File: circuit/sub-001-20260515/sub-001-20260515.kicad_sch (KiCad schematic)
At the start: 5 parts

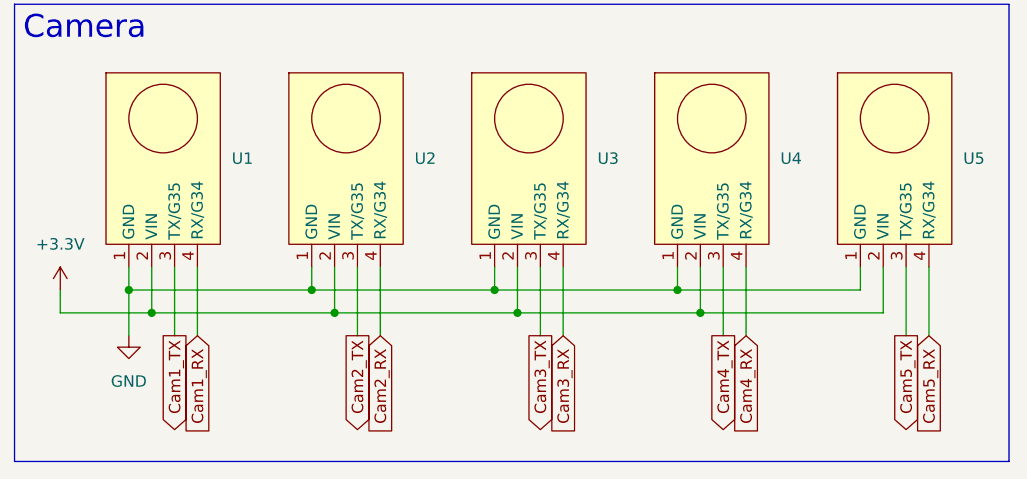
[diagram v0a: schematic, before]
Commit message: Update カメラのRX/TXを修正
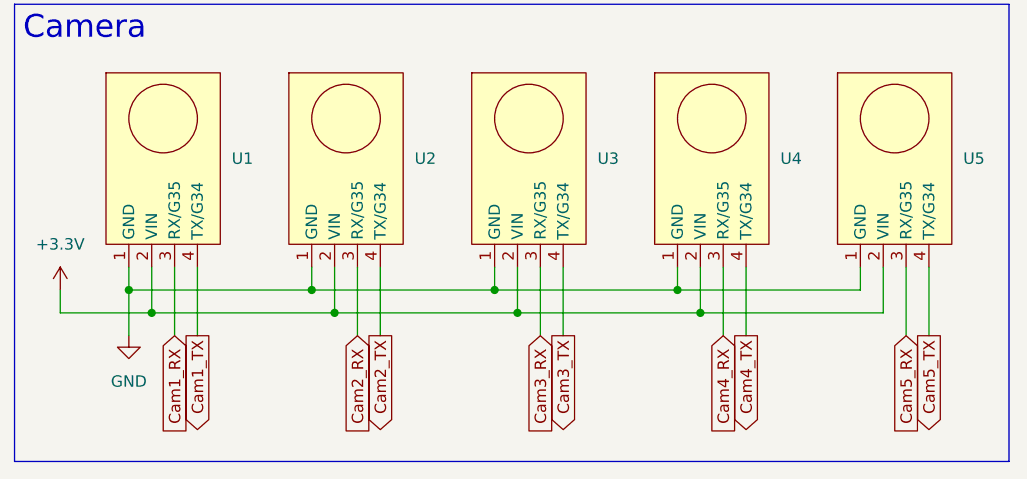
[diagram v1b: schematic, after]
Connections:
- net Cam1_RX: now also U1.3 (RX/G35); no longer U1.4 (RX/G34)
- net Cam1_TX: now also U1.4 (TX/G34); no longer U1.3 (TX/G35)
- net Cam2_RX: now also U2.3 (RX/G35); no longer U2.4 (RX/G34)
- net Cam2_TX: now also U2.4 (TX/G34); no longer U2.3 (TX/G35)
- net Cam3_RX: now also U3.3 (RX/G35); no longer U3.4 (RX/G34)
- net Cam3_TX: now also U3.4 (TX/G34); no longer U3.3 (TX/G35)
- net Cam4_RX: now also U4.3 (RX/G35); no longer U4.4 (RX/G34)
- net Cam4_TX: now also U4.4 (TX/G34); no longer U4.3 (TX/G35)
- net Cam5_RX: now also U5.3 (RX/G35); no longer U5.4 (RX/G34)
- net Cam5_TX: now also U5.4 (TX/G34); no longer U5.3 (TX/G35)
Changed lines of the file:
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@@
 	(global_label "Cam5_TX"
 		(shape output)
+		(at 114.3 49.53 270)
+		(fields_autoplaced yes)
+		(effects
+			(font
+				(size 1.27 1.27)
+			)
+			(justify right)
+		)
+		(property "Intersheetrefs" "${INTERSHEET_REFS}"
+			(at 114.3 61.3763 90)
+			(hide yes)
+			(show_name no)
+			(do_not_autoplace no)
+			(effects
+				(font
+					(size 1.27 1.27)
+				)
+				(justify right)
+			)
+		)
+	)
+	(global_label "Cam1_RX"
+		(shape input)
+		(at 30.48 49.53 270)
+		(fields_autoplaced yes)
+		(effects
+			(font
+				(size 1.27 1.27)
+			)
+			(justify right)
+		)
+		(property "Intersheetrefs" "${INTERSHEET_REFS}"
+			(at 30.48 61.4756 90)
+			(hide yes)
+			(show_name no)
+			(do_not_autoplace no)
+			(effects
+				(font
+					(size 1.27 1.27)
+				)
+				(justify right)
+			)
+		)
+	)
+	(global_label "Cam3_TX"
+		(shape output)
+		(at 73.66 49.53 270)
+		(fields_autoplaced yes)
+		(effects
+			(font
+				(size 1.27 1.27)
+			)
+			(justify right)
+		)
+		(property "Intersheetrefs" "${INTERSHEET_REFS}"
+			(at 73.66 61.3763 90)
+			(hide yes)
+			(show_name no)
+			(do_not_autoplace no)
+			(effects
+				(font
+					(size 1.27 1.27)
+				)
+				(justify right)
+			)
+		)
+	)
+	(global_label "Cam2_TX"
+		(shape output)
+		(at 53.34 49.53 270)
+		(fields_autoplaced yes)
+		(effects
+			(font
+				(size 1.27 1.27)
+			)
+			(justify right)
+		)
+		(property "Intersheetrefs" "${INTERSHEET_REFS}"
+			(at 53.34 61.3763 90)
+			(hide yes)
+			(show_name no)
+			(do_not_autoplace no)
+			(effects
+				(font
+					(size 1.27 1.27)
+				)
+				(justify right)
+			)
+		)
+	)
+	(global_label "Cam2_RX"
+		(shape input)
+		(at 50.8 49.53 270)
+		(fields_autoplaced yes)
+		(effects
+			(font
+				(size 1.27 1.27)
+			)
+			(justify right)
+		)
+		(property "Intersheetrefs" "${INTERSHEET_REFS}"
+			(at 50.8 61.4756 90)
+			(hide yes)
+			(show_name no)
+			(do_not_autoplace no)
+			(effects
+				(font
+					(size 1.27 1.27)
+				)
+				(justify right)
+			)
+		)
+	)
+	(global_label "Cam5_RX"
+		(shape input)
 		(at 111.76 49.53 270)
 		(fields_autoplaced yes)
@@
 		)
 		(property "Intersheetrefs" "${INTERSHEET_REFS}"
-			(at 111.76 61.3763 90)
-			(hide yes)
-			(show_name no)
-			(do_not_autoplace no)
-			(effects
-				(font
-					(size 1.27 1.27)
-				)
-				(justify right)
-			)
-		)
-	)
-	(global_label "Cam1_RX"
-		(shape input)
+			(at 111.76 61.4756 90)
+			(hide yes)
+			(show_name no)
+			(do_not_autoplace no)
+			(effects
+				(font
+					(size 1.27 1.27)
+				)
+				(justify right)
+			)
+		)
+	)
+	(global_label "Cam3_RX"
+		(shape input)
+		(at 71.12 49.53 270)
+		(fields_autoplaced yes)
+		(effects
+			(font
+				(size 1.27 1.27)
+			)
+			(justify right)
+		)
+		(property "Intersheetrefs" "${INTERSHEET_REFS}"
+			(at 71.12 61.4756 90)
+			(hide yes)
+			(show_name no)
+			(do_not_autoplace no)
+			(effects
+				(font
+					(size 1.27 1.27)
+				)
+				(justify right)
+			)
+		)
+	)
+	(global_label "Cam4_TX"
+		(shape output)
+		(at 93.98 49.53 270)
+		(fields_autoplaced yes)
+		(effects
+			(font
+				(size 1.27 1.27)
+			)
+			(justify right)
+		)
+		(property "Intersheetrefs" "${INTERSHEET_REFS}"
+			(at 93.98 61.3763 90)
+			(hide yes)
+			(show_name no)
+			(do_not_autoplace no)
+			(effects
+				(font
+					(size 1.27 1.27)
+				)
+				(justify right)
+			)
+		)
+	)
+	(global_label "Cam4_RX"
+		(shape input)
+		(at 91.44 49.53 270)
+		(fields_autoplaced yes)
+		(effects
+			(font
+				(size 1.27 1.27)
+			)
+			(justify right)
+		)
+		(property "Intersheetrefs" "${INTERSHEET_REFS}"
+			(at 91.44 61.4756 90)
+			(hide yes)
+			(show_name no)
+			(do_not_autoplace no)
+			(effects
+				(font
+					(size 1.27 1.27)
+				)
+				(justify right)
+			)
+		)
+	)
+	(global_label "Cam1_TX"
+		(shape output)
 		(at 33.02 49.53 270)
 		(fields_autoplaced yes)
@@
 		)
 		(property "Intersheetrefs" "${INTERSHEET_REFS}"
-			(at 33.02 61.4756 90)
-			(hide yes)
-			(show_name no)
-			(do_not_autoplace no)
-			(effects
-				(font
-					(size 1.27 1.27)
-				)
-				(justify right)
-			)
-		)
-	)
-	(global_label "Cam3_TX"
-		(shape output)
-		(at 71.12 49.53 270)
-		(fields_autoplaced yes)
-		(effects
-			(font
-				(size 1.27 1.27)
-			)
-			(justify right)
-		)
-		(property "Intersheetrefs" "${INTERSHEET_REFS}"
-			(at 71.12 61.3763 90)
-			(hide yes)
-			(show_name no)
-			(do_not_autoplace no)
-			(effects
-				(font
-					(size 1.27 1.27)
-				)
-				(justify right)
-			)
-		)
-	)
-	(global_label "Cam2_TX"
-		(shape output)
-		(at 50.8 49.53 270)
-		(fields_autoplaced yes)
-		(effects
-			(font
-				(size 1.27 1.27)
-			)
-			(justify right)
-		)
-		(property "Intersheetrefs" "${INTERSHEET_REFS}"
-			(at 50.8 61.3763 90)
-			(hide yes)
-			(show_name no)
-			(do_not_autoplace no)
-			(effects
-				(font
-					(size 1.27 1.27)
-				)
-				(justify right)
-			)
-		)
-	)
-	(global_label "Cam2_RX"
-		(shape input)
-		(at 53.34 49.53 270)
-		(fields_autoplaced yes)
-		(effects
-			(font
-				(size 1.27 1.27)
-			)
-			(justify right)
-		)
-		(property "Intersheetrefs" "${INTERSHEET_REFS}"
-			(at 53.34 61.4756 90)
-			(hide yes)
-			(show_name no)
-			(do_not_autoplace no)
-			(effects
-				(font
-					(size 1.27 1.27)
-				)
-				(justify right)
-			)
-		)
-	)
-	(global_label "Cam5_RX"
-		(shape input)
-		(at 114.3 49.53 270)
-		(fields_autoplaced yes)
-		(effects
-			(font
-				(size 1.27 1.27)
-			)
-			(justify right)
-		)
-		(property "Intersheetrefs" "${INTERSHEET_REFS}"
-			(at 114.3 61.4756 90)
-			(hide yes)
-			(show_name no)
-			(do_not_autoplace no)
-			(effects
-				(font
-					(size 1.27 1.27)
-				)
-				(justify right)
-			)
-		)
-	)
-	(global_label "Cam3_RX"
-		(shape input)
-		(at 73.66 49.53 270)
-		(fields_autoplaced yes)
-		(effects
-			(font
-				(size 1.27 1.27)
-			)
-			(justify right)
-		)
-		(property "Intersheetrefs" "${INTERSHEET_REFS}"
-			(at 73.66 61.4756 90)
-			(hide yes)
-			(show_name no)
-			(do_not_autoplace no)
-			(effects
-				(font
-					(size 1.27 1.27)
-				)
-				(justify right)
-			)
-		)
-	)
-	(global_label "Cam4_TX"
-		(shape output)
-		(at 91.44 49.53 270)
-		(fields_autoplaced yes)
-		(effects
-			(font
-				(size 1.27 1.27)
-			)
-			(justify right)
-		)
-		(property "Intersheetrefs" "${INTERSHEET_REFS}"
-			(at 91.44 61.3763 90)
-			(hide yes)
-			(show_name no)
-			(do_not_autoplace no)
-			(effects
-				(font
-					(size 1.27 1.27)
-				)
-				(justify right)
-			)
-		)
-	)
-	(global_label "Cam4_RX"
-		(shape input)
-		(at 93.98 49.53 270)
-		(fields_autoplaced yes)
-		(effects
-			(font
-				(size 1.27 1.27)
-			)
-			(justify right)
-		)
-		(property "Intersheetrefs" "${INTERSHEET_REFS}"
-			(at 93.98 61.4756 90)
-			(hide yes)
-			(show_name no)
-			(do_not_autoplace no)
-			(effects
-				(font
-					(size 1.27 1.27)
-				)
-				(justify right)
-			)
-		)
-	)
-	(global_label "Cam1_TX"
-		(shape output)
-		(at 30.48 49.53 270)
-		(fields_autoplaced yes)
-		(effects
-			(font
-				(size 1.27 1.27)
-			)
-			(justify right)
-		)
-		(property "Intersheetrefs" "${INTERSHEET_REFS}"
-			(at 30.48 61.3763 90)
-			(hide yes)
-			(show_name no)
+			(at 33.02 61.3763 90)
+			(hide yes)
+			(show_name no)

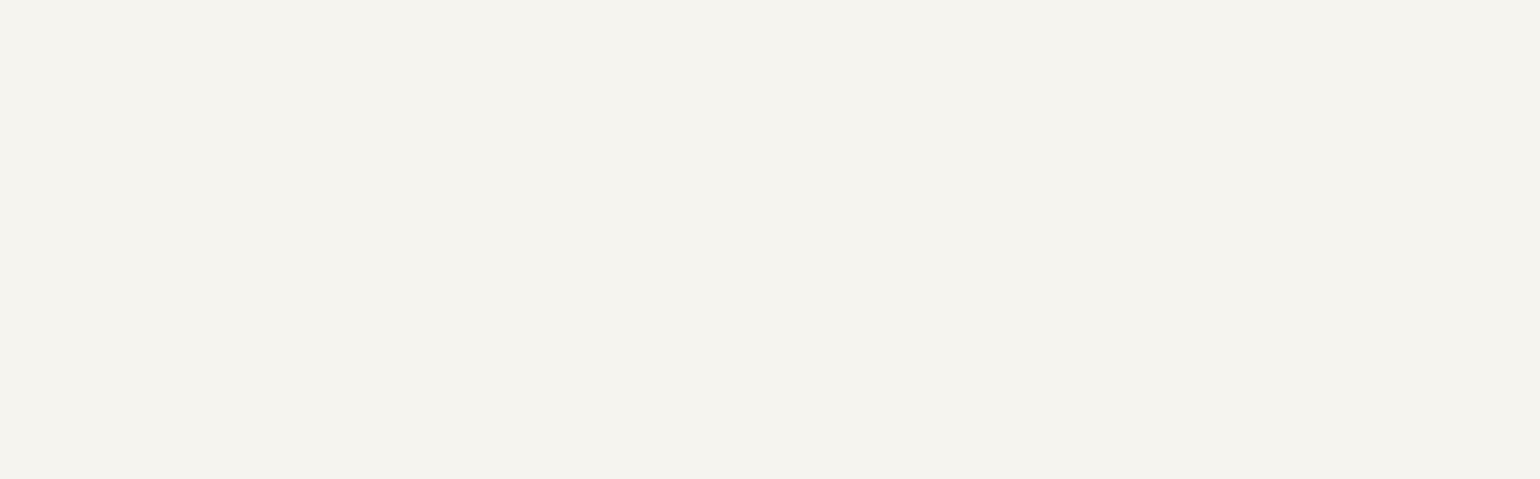
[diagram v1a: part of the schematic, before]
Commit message: Update メイン基板はピン関連とレベル変換、サブ基板はESP周りを追加した
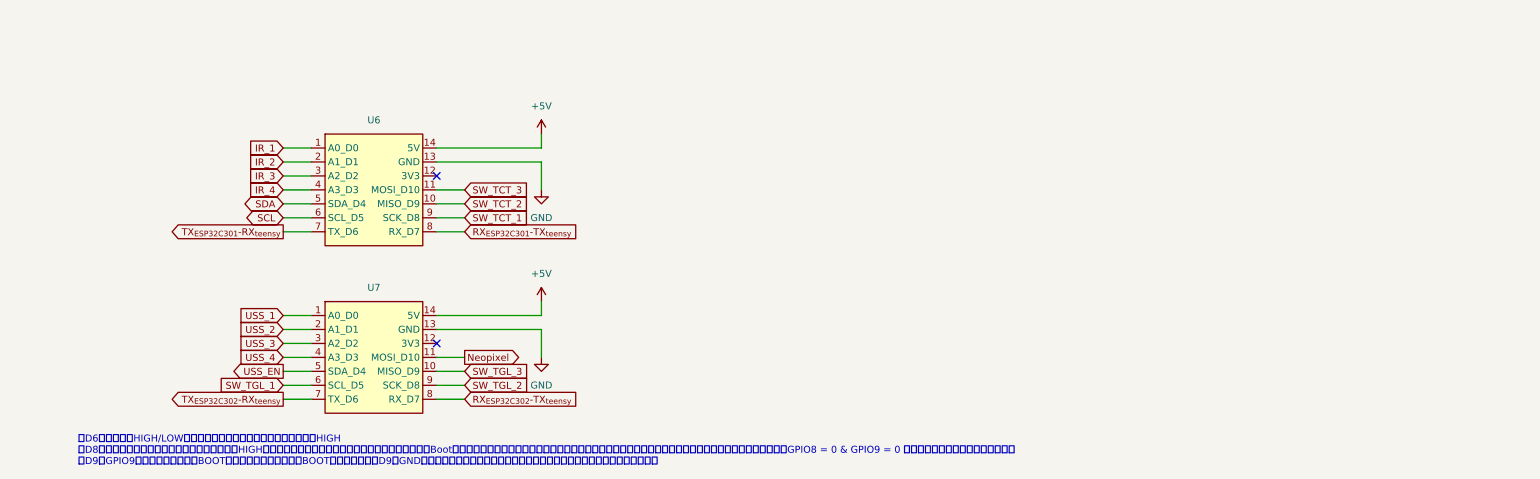
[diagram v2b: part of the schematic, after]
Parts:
- added U6, U7: (no value), symbol @Thrive_symbol_sub:XIAO_ESP32C3
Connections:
- net GND: now also U6.13 (GND), U7.13 (GND)
- new net +5V: U6.14 (5V), U7.14 (5V)
- new net IR_1: U6.1 (A0_D0)
- new net IR_2: U6.2 (A1_D1)
- new net IR_3: U6.3 (A2_D2)
- new net IR_4: U6.4 (A3_D3)
- new net Neopixel: U7.11 (MOSI_D10)
- new net RX_{ESP32C301}-TX_{teensy}: U6.8 (RX_D7)
- new net RX_{ESP32C302}-TX_{teensy}: U7.8 (RX_D7)
- new net SCL: U6.6 (SCL_D5)
- new net SDA: U6.5 (SDA_D4)
- new net SW_TCT_1: U6.9 (SCK_D8)
- new net SW_TCT_2: U6.10 (MISO_D9)
- new net SW_TCT_3: U6.11 (MOSI_D10)
- new net SW_TGL_1: U7.6 (SCL_D5)
- new net SW_TGL_2: U7.9 (SCK_D8)
- new net SW_TGL_3: U7.10 (MISO_D9)
- new net TX_{ESP32C301}-RX_{teensy}: U6.7 (TX_D6)
- new net TX_{ESP32C302}-RX_{teensy}: U7.7 (TX_D6)
- new net USS_1: U7.1 (A0_D0)
- new net USS_2: U7.2 (A1_D1)
- new net USS_3: U7.3 (A2_D2)
- new net USS_4: U7.4 (A3_D3)
- new net USS_EN: U7.5 (SDA_D4)
- no-connect marks 0 -> 2
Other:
- note added: "・D6は起動時にHIGH/LOWしてしまい、通信していない待機時は常にHIGH ・D8はプログラムの書き込みモードにした際に、HIGHになっている必要がある。書き込みモードへの移行（Bootボタンを押しながらリセットする）を行う場合は、プルアップ抵抗をつけておくのがベターだそうです。（GPIO8 = 0 & GPIO9 = 0 になると予期せぬ動きをする模様） ・D9はGPIO9とプルアップ抵抗、BOOTボタンに繋がっており、BOOTボタンを押すとD9がGNDに接続してしまうため、用途は限定的。スイッチ入力に使うのがおすすめ。"

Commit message: Update サブ基板完成した
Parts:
- added C1, C10, C11, C12, C13, C14, C2, C3, C4, C5, C6, C7, C8, C9: 10uF, symbol Device:C
- added R1, R2, R3, R4: 39k, symbol Device:R
- added R5, R6: 1k, symbol Device:R
- added SW1, SW2, SW3: SW_SPDT, symbol Switch:SW_SPDT
- added SW4, SW5, SW6: SW_SPST, symbol Switch:SW_SPST
- added U10, U11, U12, U8, U9: LD1117S12TR_SOT223, Package_TO_SOT_SMD:SOT-223-3_TabPin2, symbol Regulator_Linear:LD1117S12TR_SOT223
- added U13, U14, U15, U16: TSSP58038, OptoDevice:Vishay_MINICAST-3Pin, symbol Sensor_Proximity:TSSP58038
- added U17: (no value), symbol @Thrive_symbol_sub:SSD1306
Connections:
- net +3.3V: now also R5.2, R6.2, SW1.2 (B), SW1.3 (C), SW2.2 (B), SW2.3 (C), SW3.2 (B), SW3.3 (C), SW4.1 (A), SW5.1 (A), SW6.1 (A), U13.3 (Vs), U14.3 (Vs), U15.3 (Vs), U16.3 (Vs), U17.2 (VCC); no longer U1.2 (VIN), U2.2 (VIN), U3.2 (VIN), U4.2 (VIN), U5.2 (VIN)
- net +5V: now also C1.1, C3.1, C5.1, C7.1, C9.1, U10.3 (VI), U11.3 (VI), U12.3 (VI), U8.3 (VI), U9.3 (VI)
- net GND: now also C1.2, C10.2, C11.1, C12.1, C13.1, C14.1, C2.2, C3.2, C4.2, C5.2, C6.2, C7.2, C8.2, C9.2, U10.1 (GND), U11.1 (GND), U12.1 (GND), U13.2 (GND), U14.2 (GND), U15.2 (GND), U16.2 (GND), U17.1 (GND), U8.1 (GND), U9.1 (GND)
- net SCL: now also R6.1, U17.3 (SCL)
- net SDA: now also R5.1, U17.4 (SDA)
- net SW_TCT_1: now also SW4.2 (B)
- net SW_TCT_2: now also SW5.2 (B)
- net SW_TCT_3: now also SW6.2 (B)
- net SW_TGL_1: now also SW1.1 (A)
- net SW_TGL_2: now also SW2.1 (A)
- net SW_TGL_3: now also SW3.1 (A)
- net Cam1_RX renamed RX_{unitV1}-TX_{teensy}
- net Cam1_TX renamed TX_{unitV1}-RX_{teensy}
- net Cam2_RX renamed RX_{unitV2}-TX_{teensy}
- net Cam2_TX renamed TX_{unitV2}-RX_{teensy}
- net Cam3_RX renamed RX_{unitV3}-TX_{teensy}
- net Cam3_TX renamed TX_{unitV3}-RX_{teensy}
- net Cam4_RX renamed RX_{unitV4}-TX_{teensy}
- net Cam4_TX renamed TX_{unitV4}-RX_{teensy}
- net Cam5_RX renamed RX_{unitV5}-TX_{teensy}
- net Cam5_TX renamed TX_{unitV5}-RX_{teensy}
- net IR_1 renamed IR_sig1
- net IR_sig1: now also C11.2, R1.1
- net IR_2 renamed IR_sig2
- net IR_sig2: now also C12.2, R2.1
- net IR_3 renamed IR_sig3
- net IR_sig3: now also C13.2, R3.1
- net IR_4 renamed IR_sig4
- net IR_sig4: now also C14.2, R4.1
- new net: R2.2, U14.1 (OUT)
- new net: R4.2, U16.1 (OUT)
- new net: R1.2, U13.1 (OUT)
- new net: R3.2, U15.1 (OUT)
- new net 3.3V-unitV1: C2.1, U1.2 (VIN), U8.2 (VO)
- new net 3.3V-unitV2: C4.1, U2.2 (VIN), U9.2 (VO)
- new net 3.3V-unitV3: C6.1, U10.2 (VO), U3.2 (VIN)
- new net 3.3V-unitV4: C8.1, U11.2 (VO), U4.2 (VIN)
- new net 3.3V-unitV5: C10.1, U12.2 (VO), U5.2 (VIN)
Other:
- note added: "・D6は起動時にHIGH/LOWしてしまい、通信していない待機時は常にHIGH ・D8はプログラムの書き込みモードにした際に、HIGHになっている必要がある。 書き込みモードへの移行（Bootボタンを押しながらリセットする）を行う場合は、プルアップ抵抗をつけておくのがベターだそうです。 （GPIO8 = 0 & GPIO9 = 0 になると予期せぬ動きをする模様） ・D9はGPIO9とプルアップ抵抗、BOOTボタンに繋がっており、BOOTボタンを押すとD9がGNDに接続してしまうため、用途は限定的。 スイッチ入力に使うのがおすすめ。"
- note removed: "・D6は起動時にHIGH/LOWしてしまい、通信していない待機時は常にHIGH ・D8はプログラムの書き込みモードにした際に、HIGHになっている必要がある。書き込みモードへの移行（Bootボタンを押しながらリセットする）を行う場合は、プルアップ抵抗をつけておくのがベターだそうです。（GPIO8 = 0 & GPIO9 = 0 になると予期せぬ動きをする模様） ・D9はGPIO9とプルアップ抵抗、BOOTボタンに繋がっており、BOOTボタンを押すとD9がGNDに接続してしまうため、用途は限定的。スイッチ入力に使うのがおすすめ。"
- moved on the sheet: U6, U7

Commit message: Update サブ基板寺田DR後
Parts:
- added C15, C16, C17, C18, C19, C20, C21: 0.1uF, symbol Device:C
- added D1, D2: LED, symbol Device:LED
- added R10, R11, R12, R7, R8, R9: 10k, symbol Device:R
- added R13, R14: 330, symbol Device:R
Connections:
- net +3.3V: now also C15.1, R10.2, R11.2, R12.2, R14.1, R7.2, R8.2, R9.2; no longer SW1.2 (B), SW1.3 (C), SW2.2 (B), SW2.3 (C), SW3.2 (B), SW3.3 (C), SW4.1 (A), SW5.1 (A), SW6.1 (A)
- net +5V: now also R13.1
- net GND: now also SW1.2 (B), SW1.3 (C), SW2.2 (B), SW2.3 (C), SW3.2 (B), SW3.3 (C), SW4.1 (A), SW5.1 (A), SW6.1 (A), C15.2, C16.2, C17.2, C18.2, C19.2, C20.2, C21.2, D1.1 (K), D2.1 (K)
- net SW_TCT_1: now also C19.1, R10.1
- net SW_TCT_2: now also C20.1, R11.1
- net SW_TCT_3: now also C21.1, R12.1
- net SW_TGL_1: now also C16.1, R7.1
- net SW_TGL_2: now also C17.1, R8.1
- net SW_TGL_3: now also C18.1, R9.1
- new net: D2.2 (A), R14.2
- new net: D1.2 (A), R13.2
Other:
- moved on the sheet: C1, C10, C11, C12, C13, C14, C2, C3, C4, C5, C6, C7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

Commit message: Update サブ基板完成
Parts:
- removed C19, C20, C21: 0.1uF, symbol Device:C
- removed R12: 10k, symbol Device:R
- removed R13, R14: 330, symbol Device:R
- removed SW4, SW5, SW6: SW_SPST, symbol Switch:SW_SPST
- R10, R11: value 10k -> 330
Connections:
- net +3.3V: now also R11.1; no longer R10.2, R11.2
- net +5V: now also R10.1
- net SW_TCT_1: no longer R10.1
- net SW_TCT_2: no longer R11.1
- net at D2.2 (A): now also R11.2
- net at D1.2 (A): now also R10.2
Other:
- moved on the sheet: R10, R11
